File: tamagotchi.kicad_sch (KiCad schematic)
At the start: 1 part, among them U1 ESP32-C3

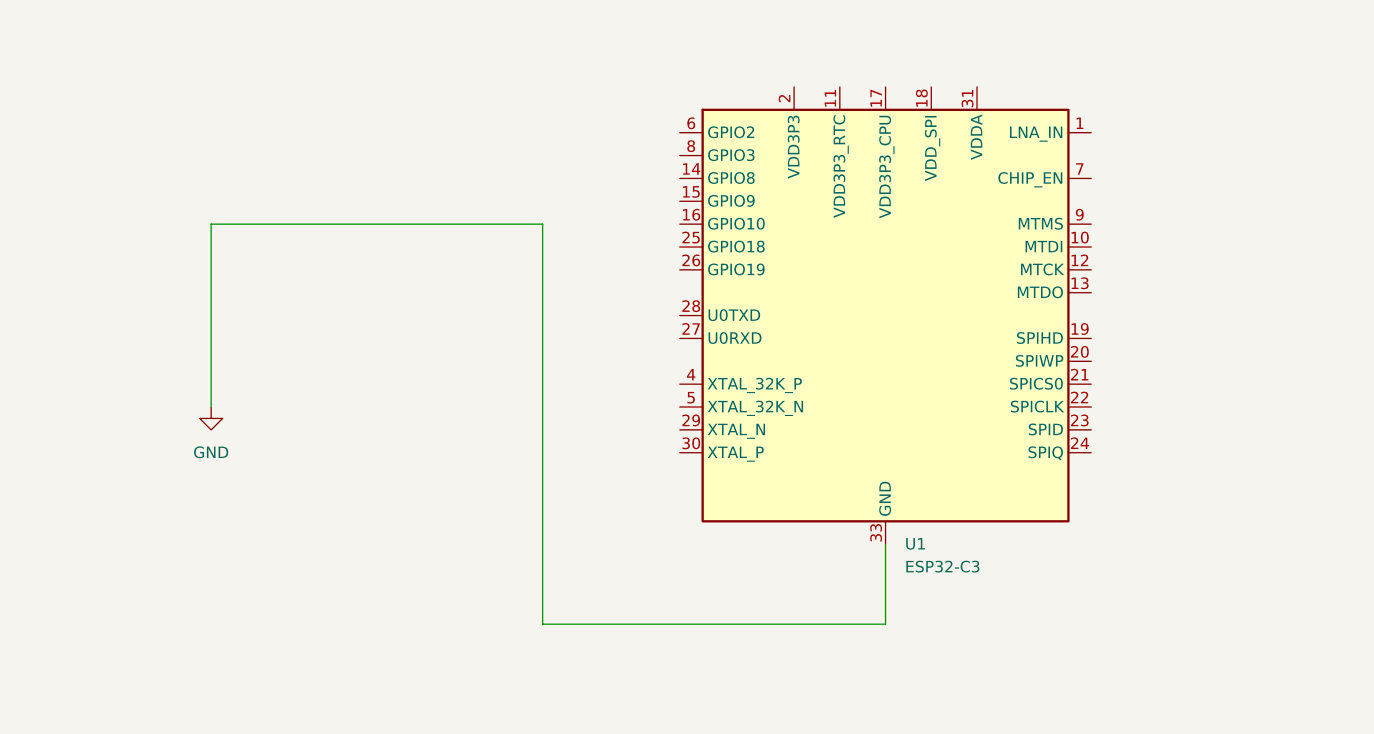
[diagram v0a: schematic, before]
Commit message: created pcb layout in pcb editor & edited push button and stuff changes
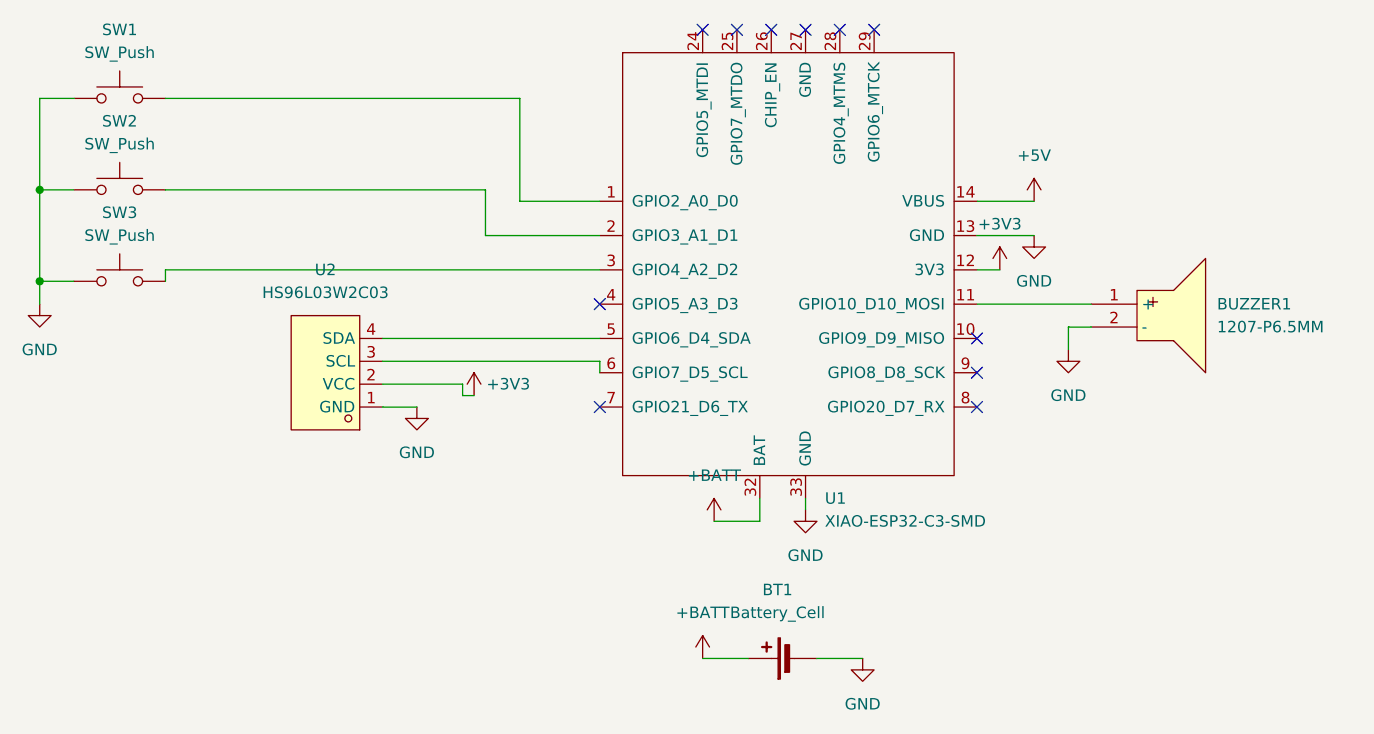
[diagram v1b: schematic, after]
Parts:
- removed U1: ESP32-C3, Package_DFN_QFN:QFN-32-1EP_5x5mm_P0.5mm_EP3.7x3.7mm, symbol MCU_Espressif:ESP32-C3
- added BT1: Battery_Cell, Connector_PinHeader_2.54mm:PinHeader_1x02_P2.54mm_Vertical, symbol Device:Battery_Cell
- added BUZZER1: 1207-P6.5MM, easyeda2kicad:BUZ-TH_BD12.5-P6.50-D1.4, symbol easyeda2kicad:1207-P6.5MM
- added SW1, SW2, SW3: SW_Push, easyeda2kicad:SW-TH_4P-L4.5-W4.5-P3.00-LS4.8, symbol Switch:SW_Push
- added U1: XIAO-ESP32-C3-SMD, Seeed_Studio_XIAO_Series:XIAO-ESP32-C3-SMD, symbol xiao_symbols:XIAO-ESP32-C3-SMD
- added U2: HS96L03W2C03, easyeda2kicad:OLED-TH_L27.8-W27.2-P2.54_C9900033791, symbol easyeda2kicad:HS96L03W2C03
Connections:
- net GND: now also BT1.2 (-), BUZZER1.2 (-), SW1.1, SW2.1, SW3.1, U1.13 (GND), U1.33 (GND), U2.1 (GND)
- new net: SW1.2, U1.1 (GPIO2_A0_D0)
- new net: BUZZER1.1 (+), U1.11 (GPIO10_D10_MOSI)
- new net: SW2.2, U1.2 (GPIO3_A1_D1)
- new net: SW3.2, U1.3 (GPIO4_A2_D2)
- new net: U1.5 (GPIO6_D4_SDA), U2.4 (SDA)
- new net: U1.6 (GPIO7_D5_SCL), U2.3 (SCL)
- new net +3V3: U1.12 (3V3), U2.2 (VCC)
- new net +5V: U1.14 (VBUS)
- new net +BATT: BT1.1 (+), U1.32 (BAT)
- no-connect marks 0 -> 11
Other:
- title: (none) -> Tamagotchi
